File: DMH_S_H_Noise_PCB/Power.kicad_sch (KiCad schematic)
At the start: 14 parts, among them J0 Conn_01x01, J100 IDC_02x08, J101 IDC_02x05

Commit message: Started schematic
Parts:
- removed C3: 47uF, Capacitor_THT:CP_Radial_D4.0mm_P1.50mm, symbol Device:C_Polarized
- removed C6: 100nF, Capacitor_THT:C_Disc_D4.3mm_W1.9mm_P5.00mm, symbol Device:C
- removed D1, D3: SB140+, Diode_THT:D_DO-41_SOD81_P10.16mm_Horizontal, symbol SynthStuff:Power_Bus_Schotty_+
- removed D2: SB140-, Diode_THT:D_DO-41_SOD81_P10.16mm_Horizontal, symbol SynthStuff:Power_Bus_Schotty_-
- removed J100: IDC_02x08, SynthStuff:IDC-Header_2x08_P2.54mm_Vertical_Eurorack, symbol SynthStuff:Eurorack_Power_Connector_16Pin
- renumbered C4 to C3, C5 to C4, J101 to J100
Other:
- note removed: "Delete what's not needed!"

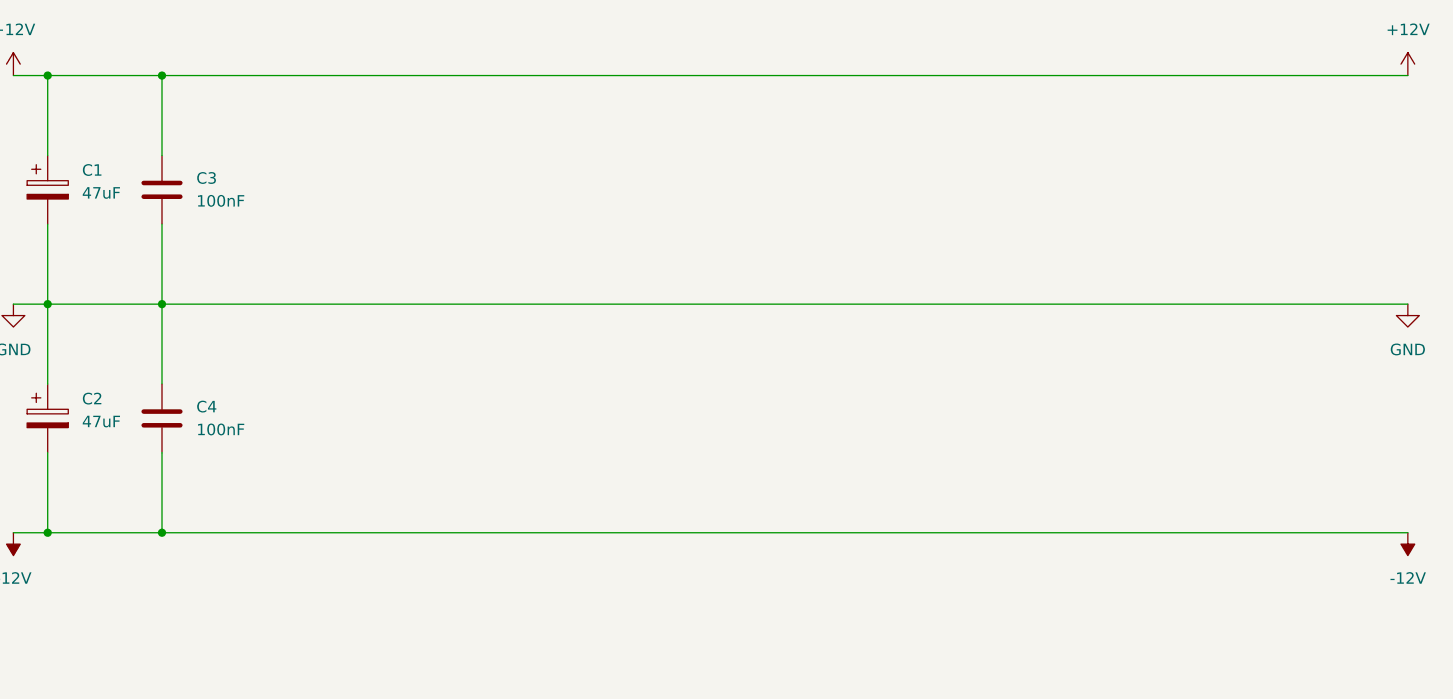
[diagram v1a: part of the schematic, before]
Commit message: Designed S&h circuit
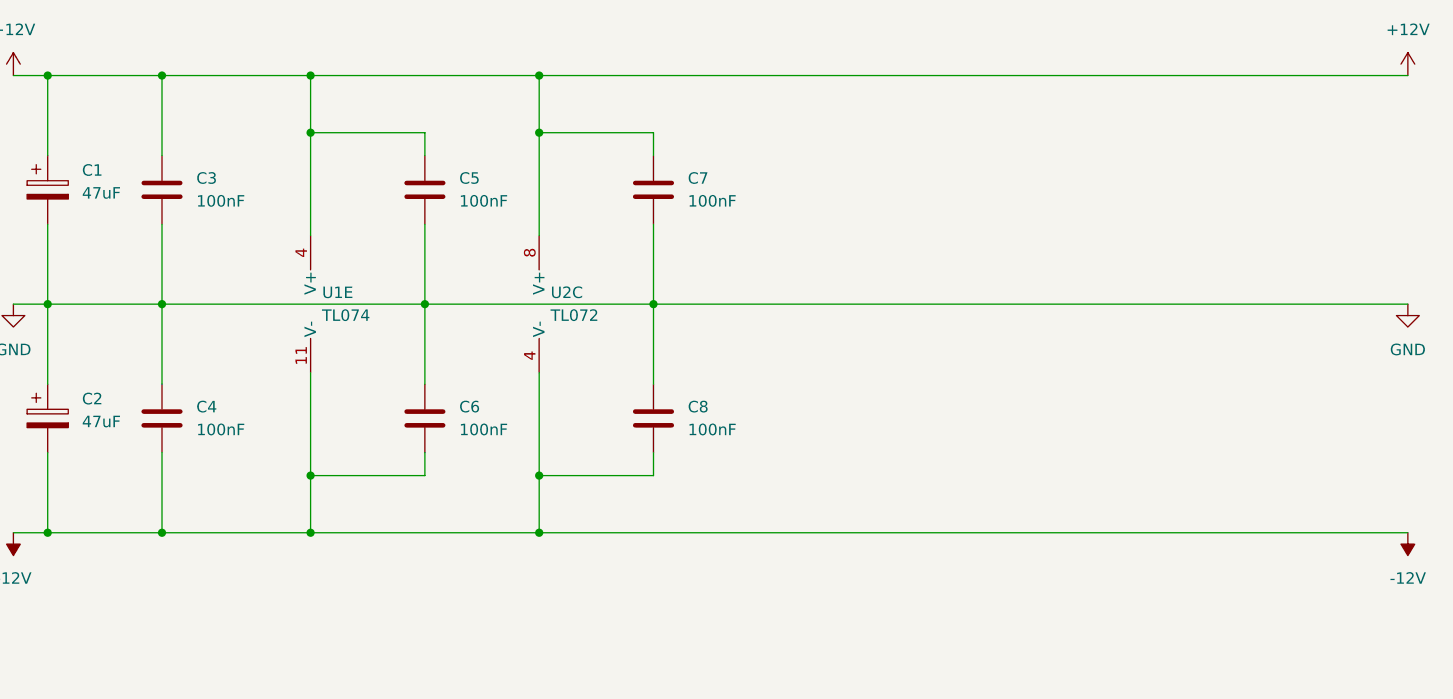
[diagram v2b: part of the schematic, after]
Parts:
- added C5, C6, C7, C8: 100nF, Capacitor_THT:C_Disc_D4.3mm_W1.9mm_P5.00mm, symbol Device:C
- added U1: TL074, Package_DIP:DIP-14_W7.62mm_Socket, symbol Amplifier_Operational:TL074
- added U2: TL072, Package_DIP:DIP-8_W7.62mm_Socket, symbol Amplifier_Operational:TL072
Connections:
- net +12V: now also C5.1, C7.1, U1.4 (V+), U2.8 (V+)
- net -12V: now also C6.2, C8.2, U1.11 (V-), U2.4 (V-)
- net GND: now also C5.2, C6.1, C7.2, C8.1

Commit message: Completed circuit
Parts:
- added C20, C21: 100nF, Capacitor_THT:C_Disc_D4.3mm_W1.9mm_P5.00mm, symbol Device:C
- added U3: TL074, Package_DIP:DIP-14_W7.62mm_Socket, symbol Amplifier_Operational:TL074
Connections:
- net +12V: now also C20.1, U3.4 (V+)
- net -12V: now also C21.2, U3.11 (V-)
- net GND: now also C20.2, C21.1

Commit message: Added clock output
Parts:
- U2: value TL072 -> TL074; footprint Package_DIP:DIP-8_W7.62mm_Socket -> Package_DIP:DIP-14_W7.62mm_Socket; symbol Amplifier_Operational:TL072 -> Amplifier_Operational:TL074
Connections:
- net +12V: now also U2.4 (V+); no longer U2.8 (V+)
- net -12V: now also U2.11 (V-); no longer U2.4 (V-)
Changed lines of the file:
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@@
 	)
 	(symbol
-		(lib_id "Amplifier_Operational:TL072")
+		(lib_id "Amplifier_Operational:TL074")
 		(at 78.74 120.65 0)
-		(unit 3)
+		(unit 5)
 		(exclude_from_sim no)
 		(in_bom yes)
@@
 			)
 		)
-		(property "Value" "TL072"
+		(property "Value" "TL074"
 			(at 77.47 121.9199 0)
 			(effects
@@
 			)
 		)
-		(property "Footprint" "Package_DIP:DIP-8_W7.62mm_Socket"
+		(property "Footprint" "Package_DIP:DIP-14_W7.62mm_Socket"
 			(at 78.74 120.65 0)
 			(effects
@@
 			)
 		)
-		(property "Description" "Dual Low-Noise JFET-Input Operational Amplifiers, DIP-8/SOIC-8"
+		(property "Description" "Quad Low-Noise JFET-Input Operational Amplifiers, DIP-14/SOIC-14"
 			(at 78.74 120.65 0)
 			(effects
@@
 				)
 				(hide yes)
+			)
+		)
+		(property "Function" ""
+			(at 78.74 120.65 0)
+			(effects
+				(font
+					(size 1.27 1.27)
+				)
 			)
 		)
@@
 		(pin "3"
 		)
+		(pin "12"
+		)
+		(pin "13"
+		)
+		(pin "10"
+		)
+		(pin "9"
+		)
+		(pin "11"
+		)
+		(pin "14"
+		)
 		(instances
 			(project "DMH_S_H_Noise_PCB"
 				(path "/58f4306d-5387-4983-bb08-41a2313fd315/0cdf34b2-39cd-4d9e-981a-97cd34791509"
 					(reference "U2")
-					(unit 3)
+					(unit 5)
 				)
 			)

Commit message: Restarted positioning from scratch
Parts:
- renumbered C21 to C10, C20 to C9, D4 to D1, D5 to D2
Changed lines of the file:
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@@
 		(dnp no)
 		(fields_autoplaced yes)
-		(property "Reference" "C20"
+		(property "Reference" "C9"
 			(at 118.11 106.6799 0)
 			(effects
@@
 			(project "DMH_S_H_Noise_PCB"
 				(path "/58f4306d-5387-4983-bb08-41a2313fd315/0cdf34b2-39cd-4d9e-981a-97cd34791509"
-					(reference "C20")
+					(reference "C9")
 					(unit 1)
 				)
@@
 		(dnp no)
 		(fields_autoplaced yes)
-		(property "Reference" "D5"
+		(property "Reference" "D2"
 			(at 113.3475 179.07 0)
 			(effects
@@
 			(project "DMH-Kosmo-5cm-PCB"
 				(path "/58f4306d-5387-4983-bb08-41a2313fd315/0cdf34b2-39cd-4d9e-981a-97cd34791509"
-					(reference "D5")
+					(reference "D2")
 					(unit 1)
 				)
@@
 		(dnp no)
 		(fields_autoplaced yes)
-		(property "Reference" "C21"
+		(property "Reference" "C10"
 			(at 118.11 132.0799 0)
 			(effects
@@
 			(project "DMH_S_H_Noise_PCB"
 				(path "/58f4306d-5387-4983-bb08-41a2313fd315/0cdf34b2-39cd-4d9e-981a-97cd34791509"
-					(reference "C21")
+					(reference "C10")
 					(unit 1)
 				)
@@
 		(dnp no)
 		(fields_autoplaced yes)
-		(property "Reference" "D4"
+		(property "Reference" "D1"
 			(at 112.7125 168.91 0)
 			(effects
@@
 			(project "DMH-Kosmo-5cm-PCB"
 				(path "/58f4306d-5387-4983-bb08-41a2313fd315/0cdf34b2-39cd-4d9e-981a-97cd34791509"
-					(reference "D4")
-					(unit 1)
-				)
+					(reference "D1")
+					(unit 1)
+				)
